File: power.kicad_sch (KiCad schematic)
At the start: 65 parts, among them Q1 CSD17303Q5, Q2 CSD17573Q5B, Q6 2N7002K, U1 LMR54410, U11 RT9080-33GJ5, U4 LM27402, U5 MIC5504, U6 DS4432U+, U6 INA219AID

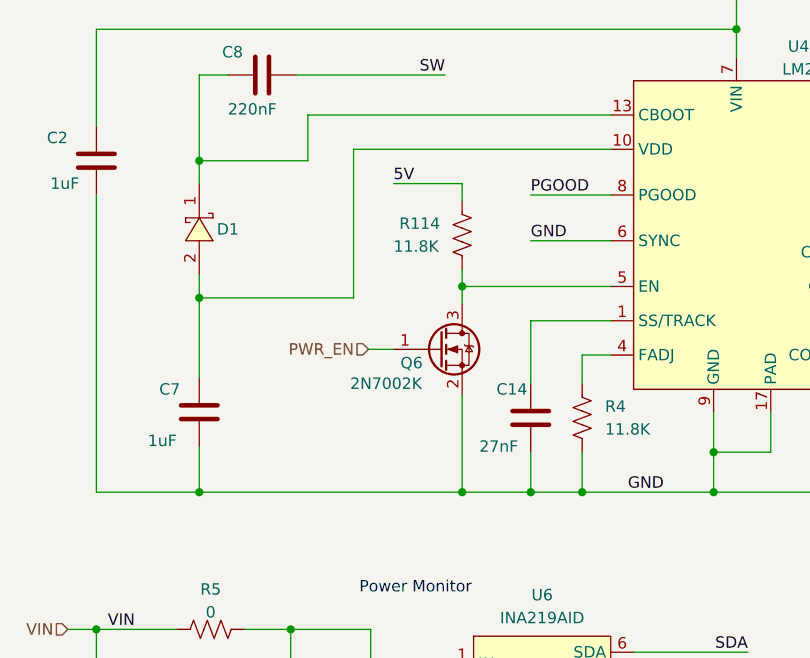
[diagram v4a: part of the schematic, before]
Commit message: More power supply routing
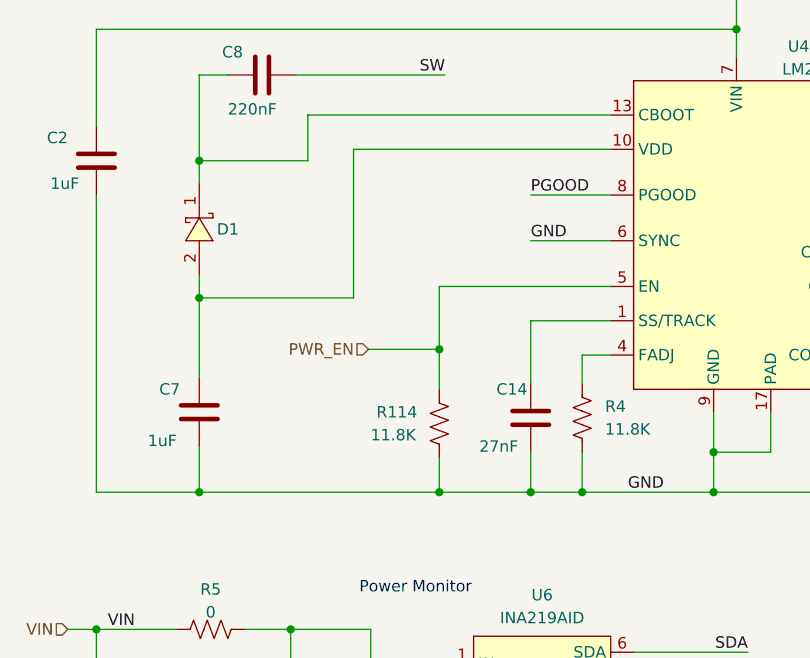
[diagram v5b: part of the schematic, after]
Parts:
- removed Q6: 2N7002K, Package_TO_SOT_SMD:SOT-323_SC-70, symbol Transistor_FET:2N7002K
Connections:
- net 5V: no longer R114.1
- net GND: now also R114.2
- net PWR_EN: now also R114.1, U4.5 (EN)
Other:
- moved on the sheet: R114
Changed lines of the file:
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@@
   (junction (at 33.02 170.815) (diameter 0) (color 0 0 0 0)
   )
+  (junction (at 68.58 79.375) (diameter 0) (color 0 0 0 0)
+  )
   (junction (at 121.285 170.815) (diameter 0) (color 0 0 0 0)
   )
@@
   (junction (at 228.6 95.25) (diameter 0) (color 0 0 0 0)
   )
-  (junction (at 71.12 72.39) (diameter 0) (color 0 0 0 0)
-  )
   (junction (at 30.48 110.49) (diameter 0) (color 0 0 0 0)
   )
@@
   (junction (at 45.72 39.37) (diameter 0) (color 0 0 0 0)
   )
+  (junction (at 68.58 95.25) (diameter 0) (color 0 0 0 0)
+  )
   (junction (at 130.175 114.935) (diameter 0) (color 0 0 0 0)
   )
@@
   )
   (junction (at 99.06 90.805) (diameter 0) (color 0 0 0 0)
-  )
-  (junction (at 71.12 95.25) (diameter 0) (color 0 0 0 0)
   )
   (junction (at 172.72 52.07) (diameter 0) (color 0 0 0 0)
@@
     (stroke (width 0) (type default))
   )
-  (wire (pts (xy 41.91 95.25) (xy 71.12 95.25))
-    (stroke (width 0) (type default))
-  )
   (wire (pts (xy 45.72 22.86) (xy 45.72 27.94))
     (stroke (width 0) (type default))
@@
     (stroke (width 0) (type default))
   )
+  (wire (pts (xy 68.58 72.39) (xy 87.63 72.39))
+    (stroke (width 0) (type default))
+  )
   (wire (pts (xy 242.57 139.065) (xy 242.57 144.145))
     (stroke (width 0) (type default))
@@
     (stroke (width 0) (type default))
   )
-  (wire (pts (xy 71.12 62.865) (xy 71.12 60.96))
-    (stroke (width 0) (type default))
-  )
   (wire (pts (xy 139.7 40.005) (xy 139.7 45.72))
     (stroke (width 0) (type default))
   )
-  (wire (pts (xy 60.706 79.375) (xy 63.5 79.375))
+  (wire (pts (xy 60.706 79.375) (xy 68.58 79.375))
     (stroke (width 0) (type default))
   )
@@
     (stroke (width 0) (type default))
   )
-  (wire (pts (xy 71.12 84.455) (xy 71.12 95.25))
-    (stroke (width 0) (type default))
-  )
   (wire (pts (xy 209.55 130.175) (xy 212.725 130.175))
     (stroke (width 0) (type default))
@@
     (stroke (width 0) (type default))
   )
-  (wire (pts (xy 87.63 72.39) (xy 71.12 72.39))
-    (stroke (width 0) (type default))
-  )
   (wire (pts (xy 68.58 121.92) (xy 69.85 121.92))
     (stroke (width 0) (type default))
@@
     (stroke (width 0) (type default))
   )
-  (wire (pts (xy 71.12 60.96) (xy 63.5 60.96))
-    (stroke (width 0) (type default))
-  )
   (wire (pts (xy 130.175 80.01) (xy 136.525 80.01))
     (stroke (width 0) (type default))
   )
+  (wire (pts (xy 68.58 95.25) (xy 78.74 95.25))
+    (stroke (width 0) (type default))
+  )
   (wire (pts (xy 194.945 45.72) (xy 215.9 45.72))
     (stroke (width 0) (type default))
@@
     (stroke (width 0) (type default))
   )
+  (wire (pts (xy 68.58 91.44) (xy 68.58 95.25))
+    (stroke (width 0) (type default))
+  )
   (wire (pts (xy 87.63 57.15) (xy 59.055 57.15))
     (stroke (width 0) (type default))
@@
     (stroke (width 0) (type default))
   )
+  (wire (pts (xy 68.58 83.82) (xy 68.58 79.375))
+    (stroke (width 0) (type default))
+  )
   (wire (pts (xy 41.91 71.12) (xy 41.91 73.66))
     (stroke (width 0) (type default))
@@
     (stroke (width 0) (type default))
   )
-  (wire (pts (xy 71.12 95.25) (xy 78.74 95.25))
+  (wire (pts (xy 41.91 95.25) (xy 68.58 95.25))
     (stroke (width 0) (type default))
   )
@@
     (stroke (width 0) (type default))
   )
-  (wire (pts (xy 71.12 72.39) (xy 71.12 74.295))
-    (stroke (width 0) (type default))
-  )
   (wire (pts (xy 33.02 170.815) (xy 42.545 170.815))
     (stroke (width 0) (type default))
@@
     (stroke (width 0) (type default))
   )
+  (wire (pts (xy 68.58 79.375) (xy 68.58 72.39))
+    (stroke (width 0) (type default))
+  )
   (wire (pts (xy 233.68 130.175) (xy 233.68 131.445))
     (stroke (width 0) (type default))
@@
   )
   (wire (pts (xy 228.6 45.72) (xy 228.6 58.42))
-    (stroke (width 0) (type default))
-  )
-  (wire (pts (xy 71.12 70.485) (xy 71.12 72.39))
     (stroke (width 0) (type default))
   )
@@
   )
   (label "VIN_M" (at 31.75 128.905 0) (fields_autoplaced)
-    (effects (font (size 1.27 1.27)) (justify left bottom))
-  )
-  (label "5V" (at 63.5 60.96 0) (fields_autoplaced)
     (effects (font (size 1.27 1.27)) (justify left bottom))
   )
@@
     )
   )
-  (symbol (lib_id "Transistor_FET:2N7002K") (at 68.58 79.375 0) (unit 1)
-    (in_bom yes) (on_board yes) (dnp no)
-    (property "Reference" "Q6" (at 64.262 80.899 0)
-      (effects (font (size 1.27 1.27)) (justify left))
-    )
-    (property "Value" "2N7002K" (at 58.674 83.185 0)
-      (effects (font (size 1.27 1.27)) (justify left))
-    )
-    (property "Footprint" "Package_TO_SOT_SMD:SOT-323_SC-70" (at 73.66 81.28 0)
-      (effects (font (size 1.27 1.27) italic) (justify left) hide)
-    )
-    (property "Datasheet" "https://www.diodes.com/assets/Datasheets/ds30896.pdf" (at 68.58 79.375 0)
-      (effects (font (size 1.27 1.27)) (justify left) hide)
-    )
-    (property "DK" "2N7002KWCT-ND" (at 68.58 79.375 0)
-      (effects (font (size 1.27 1.27)) hide)
-    )
-    (property "PARTNO" "2N7002KW" (at 68.58 79.375 0)
-      (effects (font (size 1.27 1.27)) hide)
-    )
-    (pin "1")
-    (pin "2")
-    (pin "3")
-    (instances
-      (project "bitaxeHex"
-        (path "/e63e39d7-6ac0-4ffd-8aa3-1841a4541b55/8ec0a9c6-2b78-44ef-a83d-9047d2828409"
-          (reference "Q6") (unit 1)
-        )
-      )
-    )
-  )
   (symbol (lib_id "bitaxe:MIC5504") (at 141.605 147.955 0) (unit 1)
     (in_bom yes) (on_board yes) (dnp no) (fields_autoplaced)
@@
     )
   )
-  (symbol (lib_id "Device:R_US") (at 71.12 66.675 0) (unit 1)
-    (in_bom yes) (on_board yes) (dnp no)
-    (property "Reference" "R114" (at 64.135 65.405 0)
-      (effects (font (size 1.27 1.27)) (justify left))
-    )
-    (property "Value" "11.8K" (at 63.5 67.945 0)
-      (effects (font (size 1.27 1.27)) (justify left))
-    )
-    (property "Footprint" "Resistor_SMD:R_0402_1005Metric" (at 72.136 66.929 90)
-      (effects (font (size 1.27 1.27)) hide)
-    )
-    (property "Datasheet" "~" (at 71.12 66.675 0)
-      (effects (font (size 1.27 1.27)) hide)
-    )
-    (property "DK" "YAG2958CT-ND" (at 71.12 66.675 0)
-      (effects (font (size 1.27 1.27)) hide)
-    )
-    (property "PARTNO" "RC0402FR-0711K8L" (at 71.12 66.675 0)
-      (effects (font (size 1.27 1.27)) hide)
-    )
+  (symbol (lib_id "Device:R_US") (at 68.58 87.63 0) (unit 1)
+    (in_bom yes) (on_board yes) (dnp no)
+    (property "Reference" "R114" (at 61.595 86.36 0)
+      (effects (font (size 1.27 1.27)) (justify left))
+    )
+    (property "Value" "11.8K" (at 60.96 88.9 0)
+      (effects (font (size 1.27 1.27)) (justify left))
+    )
+    (property "Footprint" "Resistor_SMD:R_0402_1005Metric" (at 69.596 87.884 90)
+      (effects (font (size 1.27 1.27)) hide)
+    )
+    (property "Datasheet" "~" (at 68.58 87.63 0)
+      (effects (font (size 1.27 1.27)) hide)
+    )
+    (property "DK" "YAG2958CT-ND" (at 68.58 87.63 0)
+      (effects (font (size 1.27 1.27)) hide)
+    )
+    (property "PARTNO" "RC0402FR-0711K8L" (at 68.58 87.63 0)
+      (effects (font (size 1.27 1.27)) hide)
+    )

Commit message: Finished routing, generate gerbers, edit new BOM for v301
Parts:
- R112: DK (none) -> YAG2956CT-ND; PARTNO (none) -> RC0402FR-07115KL
- R113: DK (none) -> 311-22.1KLRCT-ND; PARTNO (none) -> RC0402FR-0722K1L
- U1: PARTNO (none) -> LMR54410FDBVR; partnum LMR54410FDBVR -> (none)
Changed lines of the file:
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@@
       (effects (font (size 1.27 1.27)) hide)
     )
-    (property "partnum" "LMR54410FDBVR" (at 73.025 169.545 0)
+    (property "PARTNO" "LMR54410FDBVR" (at 73.025 169.545 0)
       (effects (font (size 1.27 1.27)) hide)
     )
@@
       (effects (font (size 1.27 1.27)) hide)
     )
-    (property "DK" "" (at 109.22 189.23 0)
-      (effects (font (size 1.27 1.27)) hide)
-    )
-    (property "PARTNO" "" (at 109.22 189.23 0)
+    (property "DK" "311-22.1KLRCT-ND" (at 109.22 189.23 0)
+      (effects (font (size 1.27 1.27)) hide)
+    )
+    (property "PARTNO" "RC0402FR-0722K1L" (at 109.22 189.23 0)
       (effects (font (size 1.27 1.27)) hide)
     )
@@
       (effects (font (size 1.27 1.27)) hide)
     )
-    (property "DK" "" (at 109.22 177.8 0)
-      (effects (font (size 1.27 1.27)) hide)
-    )
-    (property "PARTNO" "" (at 109.22 177.8 0)
-      (effects (font (size 1.27 1.27)) hide)
-    )
+    (property "DK" "YAG2956CT-ND" (at 109.22 177.8 0)
+      (effects (font (size 1.27 1.27)) hide)
+    )
+    (property "PARTNO" "RC0402FR-07115KL" (at 109.22 177.8 0)
+      (effects (font (size 1.27 1.27)) hide)
+    )

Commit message: fix LM27402 footprint
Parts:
- U4: footprint Package_DFN_QFN:WQFN-16-1EP_4x4mm_P0.5mm_EP2.6x2.6mm_ThermalVias -> bitaxe:SQB16A
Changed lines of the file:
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@@
       (effects (font (size 1.27 1.27)) (justify left))
     )
-    (property "Footprint" "Package_DFN_QFN:WQFN-16-1EP_4x4mm_P0.5mm_EP2.6x2.6mm_ThermalVias" (at 101.6 38.1 0)
+    (property "Footprint" "bitaxe:SQB16A" (at 101.6 38.1 0)
       (effects (font (size 1.27 1.27)) hide)
     )

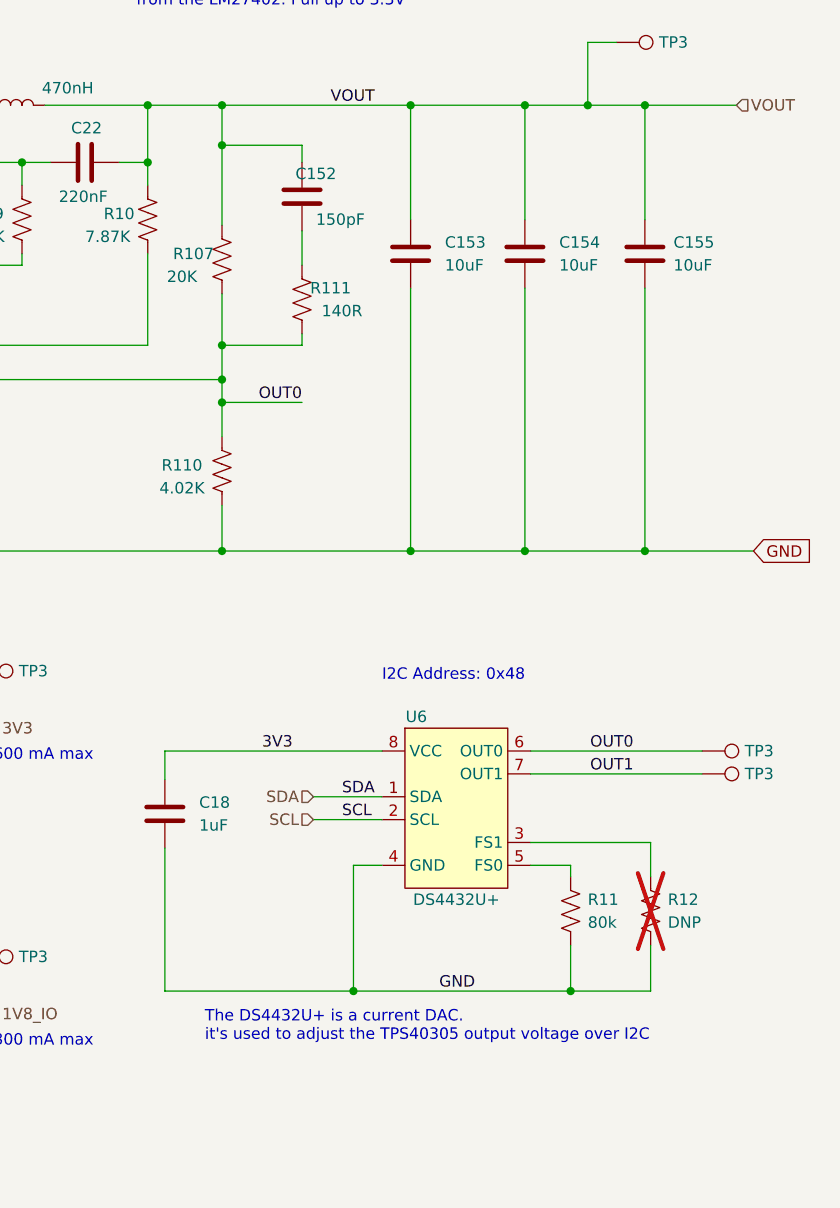
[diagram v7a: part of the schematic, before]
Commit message: fix warnings on H3 and H4 mounting holes
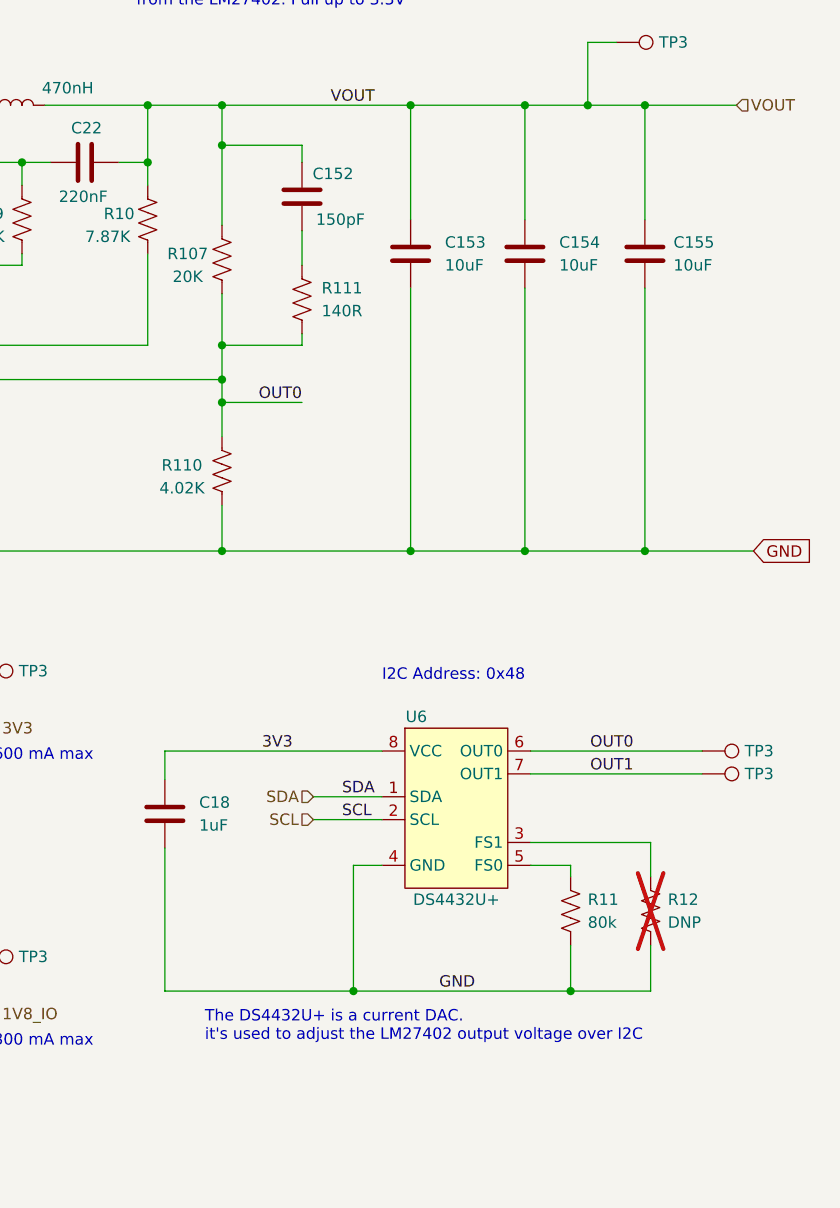
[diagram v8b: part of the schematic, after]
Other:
- note added: "The DS4432U+ is a current DAC. it's used to adjust the LM27402 output voltage over I2C"
- note removed: "The DS4432U+ is a current DAC. it's used to adjust the TPS40305 output voltage over I2C"
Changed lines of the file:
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@@
     (effects (font (size 1.27 1.27)) (justify left bottom))
   )
-  (text "The DS4432U+ is a current DAC. \nit's used to adjust the TPS40305 output voltage over I2C"
+  (text "The DS4432U+ is a current DAC. \nit's used to adjust the LM27402 output voltage over I2C"
     (at 193.04 149.86 0)
     (effects (font (size 1.27 1.27)) (justify left bottom))
@@
   (symbol (lib_id "Device:C") (at 203.835 55.88 180) (unit 1)
     (in_bom yes) (on_board yes) (dnp no)
-    (property "Reference" "C152" (at 207.645 53.34 0)
+    (property "Reference" "C152" (at 209.55 53.34 0)
       (effects (font (size 1.27 1.27)) (justify left))
     )
@@
   (symbol (lib_id "Device:R_US") (at 194.945 62.865 180) (unit 1)
     (in_bom yes) (on_board yes) (dnp no)
-    (property "Reference" "R107" (at 191.77 62.23 0)
-      (effects (font (size 1.27 1.27)))
-    )
-    (property "Value" "20K" (at 190.5 64.77 0)
+    (property "Reference" "R107" (at 191.135 62.23 0)
+      (effects (font (size 1.27 1.27)))
+    )
+    (property "Value" "20K" (at 191.135 64.77 0)
       (effects (font (size 1.27 1.27)))
     )
@@
   (symbol (lib_id "Device:R_US") (at 203.835 67.31 180) (unit 1)
     (in_bom yes) (on_board yes) (dnp no)
-    (property "Reference" "R111" (at 207.01 66.04 0)
-      (effects (font (size 1.27 1.27)))
-    )
+    (property "Reference" "R111" (at 208.28 66.04 0)
+      (effects (font (size 1.27 1.27)))
+    )
